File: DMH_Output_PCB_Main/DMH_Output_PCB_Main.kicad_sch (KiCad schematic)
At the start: 14 parts, among them J1 TRS_Jack_6.35mm_Sw, J2 TRS_Jack_6.35mm_Sw, J200 IDC_02x05, J21 Conn_01x02, J22 Conn_01x02, J24 Conn_01x02, J25 Conn_01x02, J3 TRS_Jack_6.35mm_Sw, J4 TRS_Jack_6.35mm_Sw, J5 TRS_Jack_6.35mm_Sw, J6 TRS_Jack_6.35mm_Sw, J7 TRS_Jack_6.35mm_Sw, J8 TRS_Jack_6.35mm_Sw, J9 TRS_Jack_6.35mm_Sw

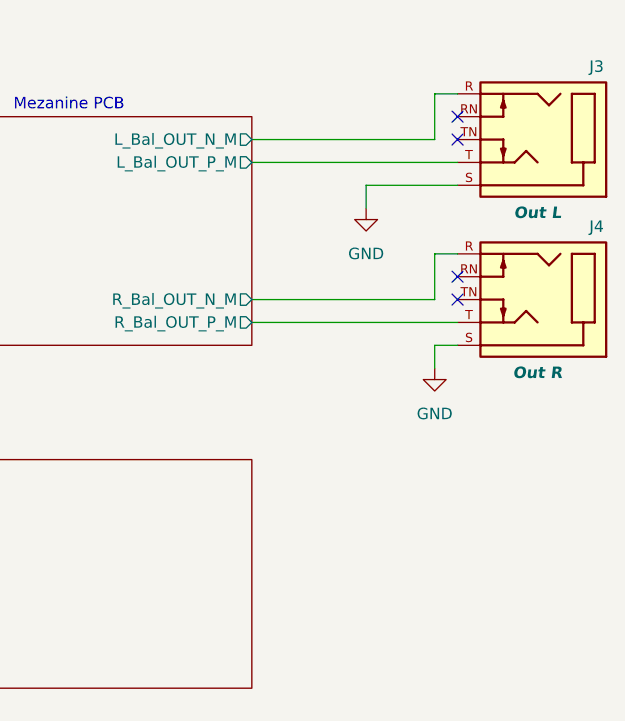
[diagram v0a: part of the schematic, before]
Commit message: Added test points for easier calibration
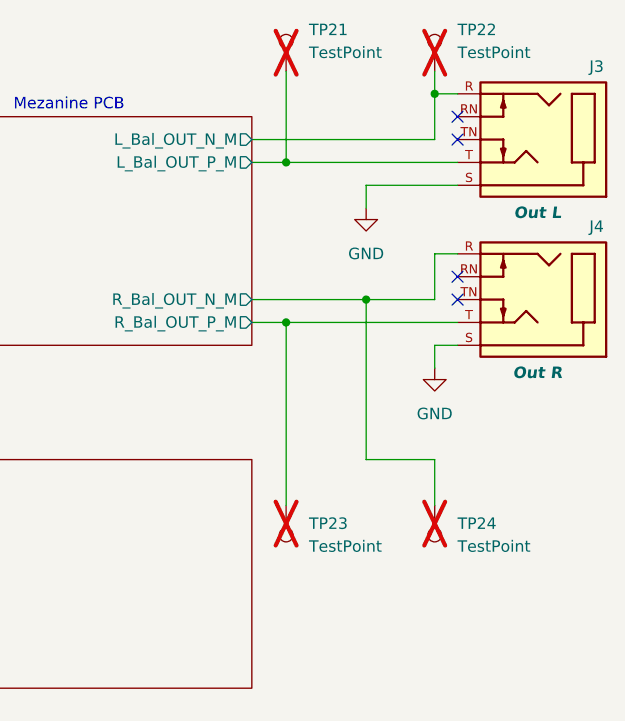
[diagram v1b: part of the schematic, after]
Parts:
- added TP21, TP22, TP23, TP24: TestPoint, Connector_Pin:Pin_D1.0mm_L10.0mm, symbol Connector:TestPoint
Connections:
- net Balanced Line Driver/L_Bal_OUT_N_M: now also TP22.1
- net Balanced Line Driver/L_Bal_OUT_P_M: now also TP21.1
- net Balanced Line Driver/R_Bal_OUT_N_M: now also TP24.1
- net Balanced Line Driver/R_Bal_OUT_P_M: now also TP23.1

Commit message: Exported BoM and Schematic
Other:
- title: (none) -> 5532 Output
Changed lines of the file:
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@@
 	(paper "A4")
 	(title_block
+		(title "5532 Output")
+		(date "2026-07-09")
 		(rev "1")
 		(company "DMH Instruments")
-		(comment 1 "PCB for 5 cm Kosmo format synthesizer module")
+		(comment 1 "5 cm Kosmo format synthesizer module")
 	)
 	(rectangle
